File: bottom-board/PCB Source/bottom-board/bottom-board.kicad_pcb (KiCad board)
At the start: 4 copper layers, 193 x 93 mm, 307 parts, among them J1 AS0A823-H4SB-7H, P1 USB_B, P10 JACK_TRS_6PINS, P11 JACK_TRS_6PINS, P12 JACK_TRS_6PINS, P13 RJ45, P14 AudioJack3, P2 USB_A, P3 BARREL_JACK, P5 HMI_DATA, P6 AudioJack3, P7 AudioJack3, P8 SERIAL_DEBUG, P9 JACK_TRS_6PINS, Q1 2N7002, Q10 MMBFJ111, Q12 2N7002, Q13 2N7002, Q2 2N7002, Q3 MMBFJ111, Q4 MMBFJ111, Q5 MMBFJ111, Q6 MMBFJ111, Q7 2N7002, Q8 2N7002, Q9 MMBFJ111, U1 TS2596, U10 TPS2001DDBVR, U11 6N137S, U12 ISL83491, U13 AP2120N-3.3, U2 TL750M10CKVURG3, U3 CS4265, U4 AT24CS08-STUM, U5 LM4562, U6 OPA1678, U7 OPA1678, U8 LM4811, U9 LD1117S50TR_SOT223, X1 24.576MHz

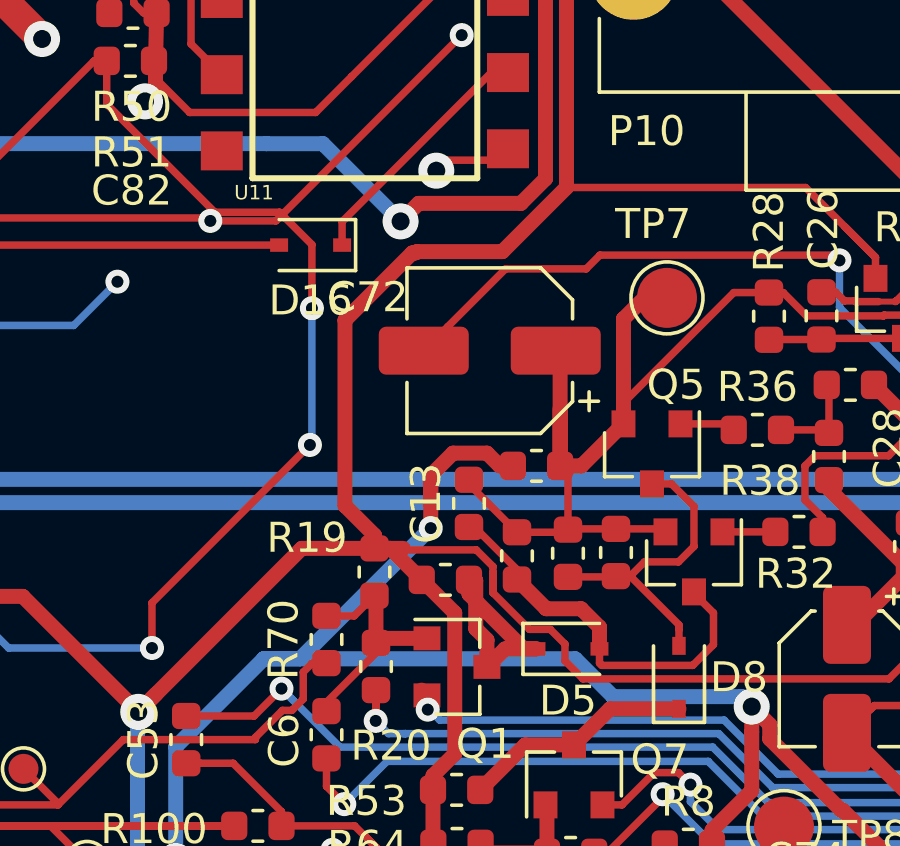
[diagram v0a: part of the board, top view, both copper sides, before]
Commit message: change input bias from 5 to 6 volts
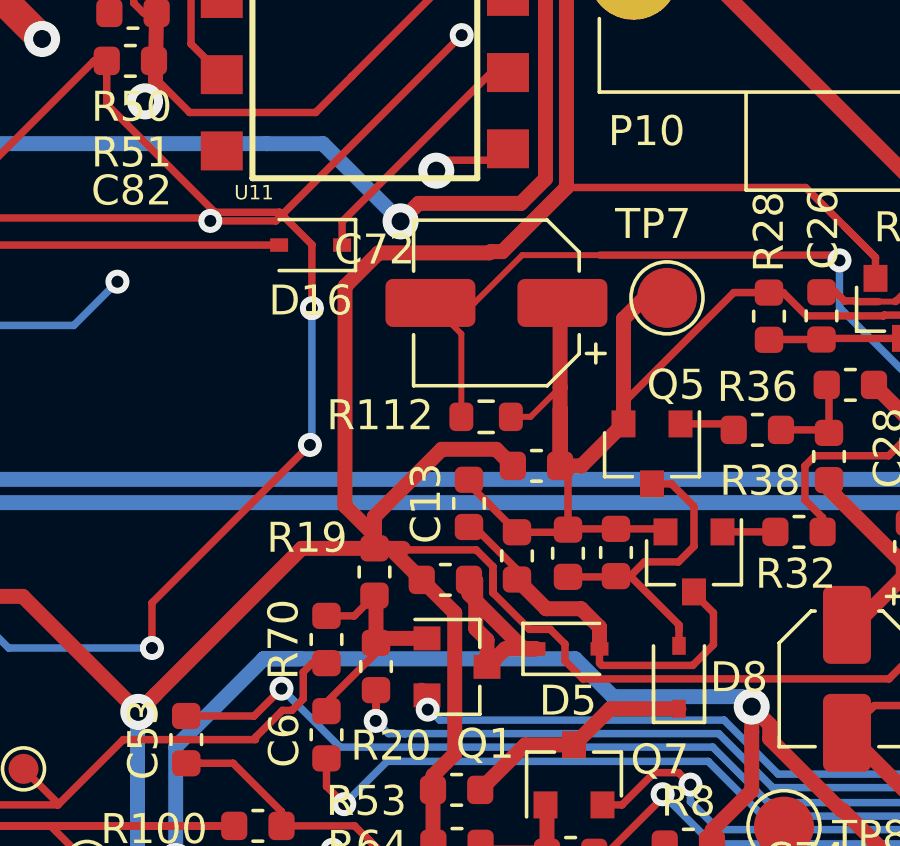
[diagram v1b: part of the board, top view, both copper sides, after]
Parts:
- added R112: 1K, Resistor_SMD:R_0603_1608Metric, F.Cu at (202.6, 75.9)
- C21, C23: value 100nF -> 100pF
- Q10, Q3, Q4, Q5, Q6, Q9: value MMBFJ111 -> MMBFJ110
- R101: value 100R -> 1K
- moved C72 1.61 mm to (202.9, 72.1)
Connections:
- R101 pad 2: +5VA -> +10V
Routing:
- net +5VA: track 290.0 -> 277.8 mm, vias 15 -> 14
- net +10V: track 311.8 -> 319.3 mm
- net INPUT_BIAS: track 88.5 -> 92.1 mm
- net GNDA: track 3561.3 -> 3564.7 mm

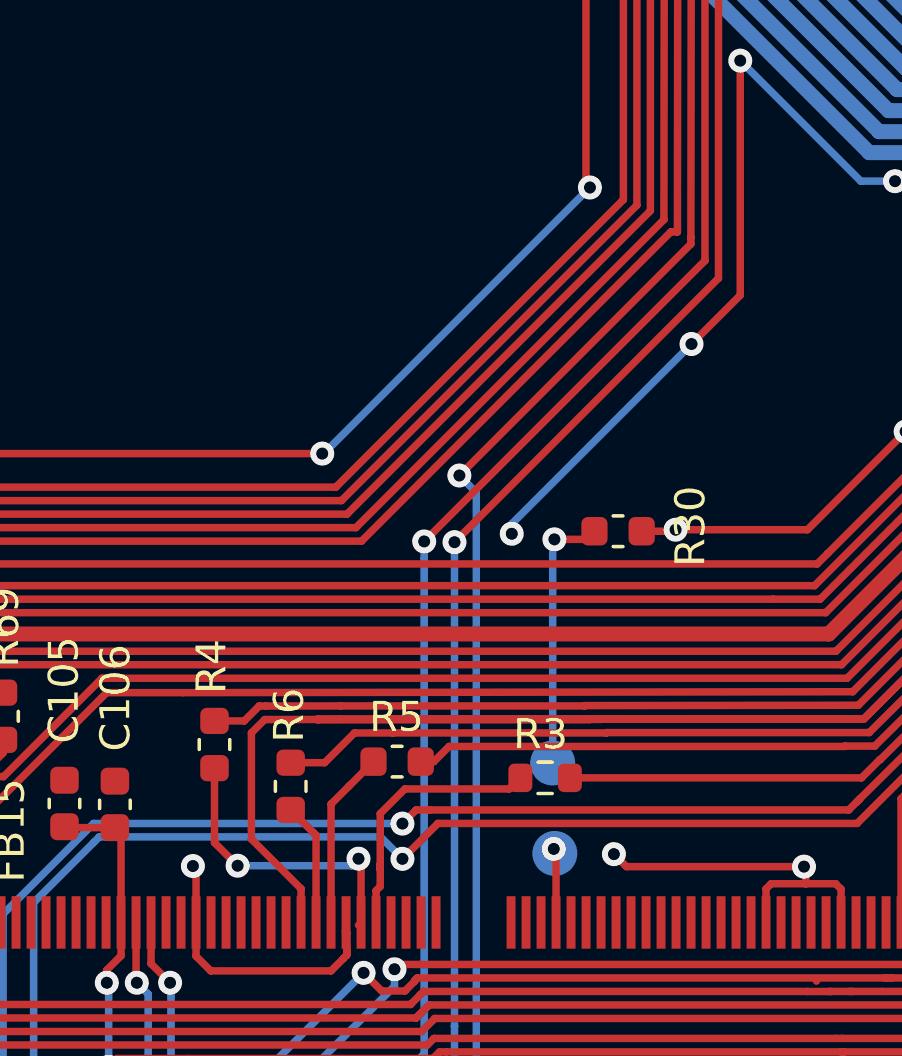
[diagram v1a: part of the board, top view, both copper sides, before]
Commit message: change recovery pads to holes, easier on production
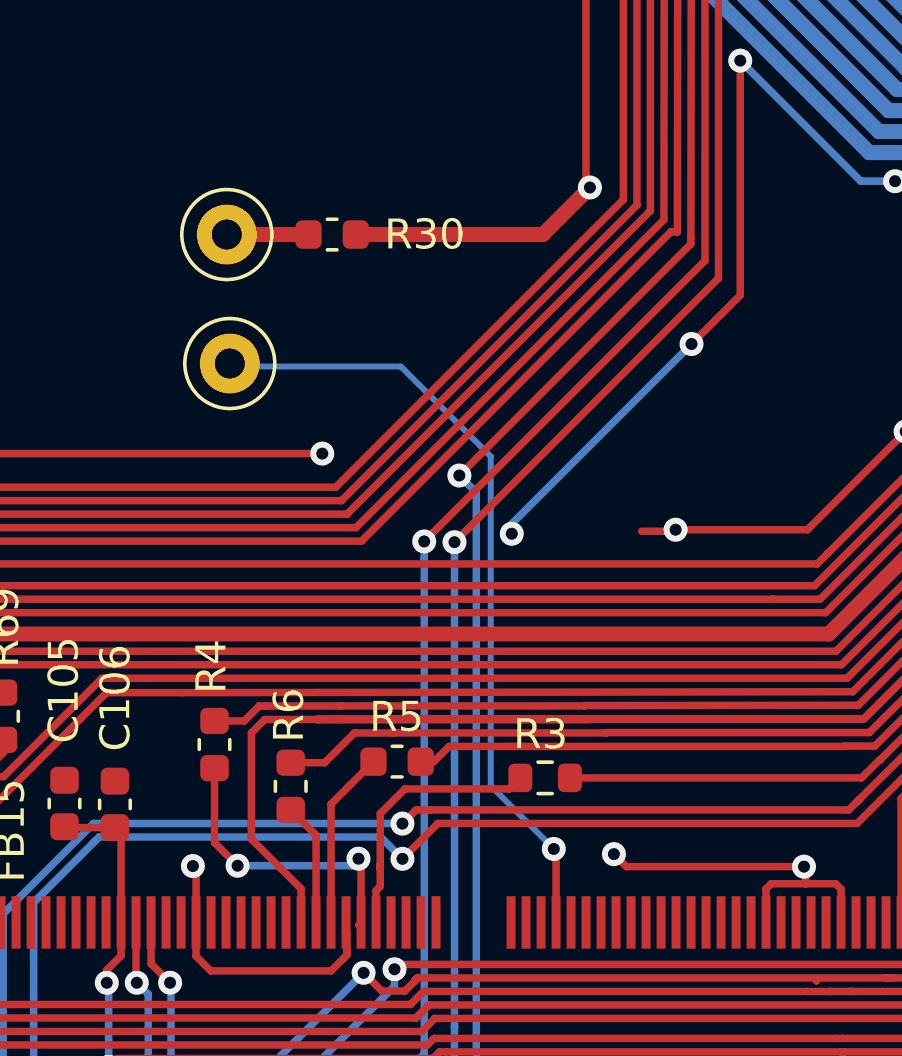
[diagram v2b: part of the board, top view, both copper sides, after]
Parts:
- removed Reset1: TestPoint, TestPoint:TestPoint_Pad_D1.5mm
- added Reset: TestPoint, TestPoint:TestPoint_Pad_D1.5mm, B.Cu at (120.3, 130.3)
- TP1, TP2: footprint TestPoint:TestPoint_Pad_D1.5mm -> TestPoint:TestPoint_Loop_D1.80mm_Drill1.0mm_Beaded; moved to F.Cu
- moved TP2 20.7 mm to (98.2, 101.2)
- moved TP1 19.6 mm to (98.3, 105.5)
- moved R30 13.7 mm to (101.7, 101.2)
- renumbered Power1 to Power
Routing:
- net UBOOT_BUTTON: track 2.50 -> 26.8 mm
- net Net-(R30-Pad2): track 8.93 -> 3.12 mm, vias 1 -> 0
- net GNDD: track 1451.8 -> 1447.7 mm

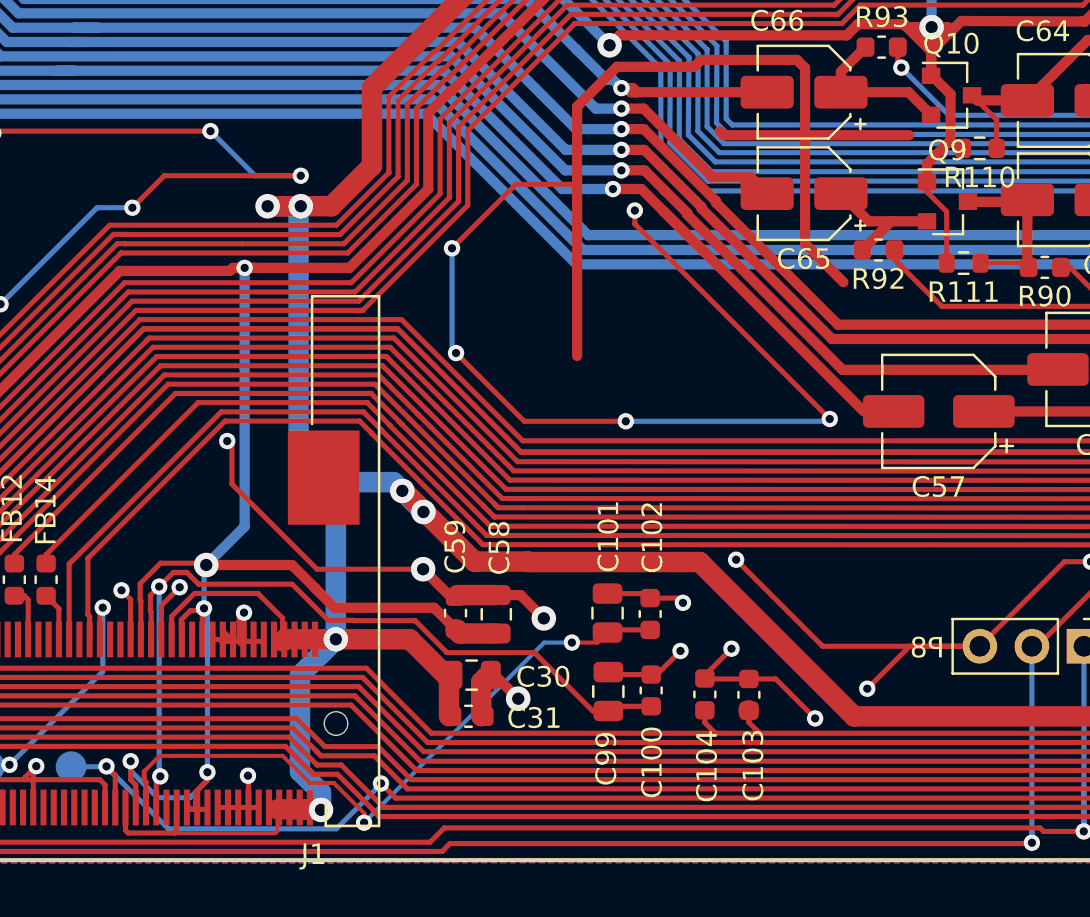
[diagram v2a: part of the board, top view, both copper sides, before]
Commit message: give analog bias to PX30 analog reference
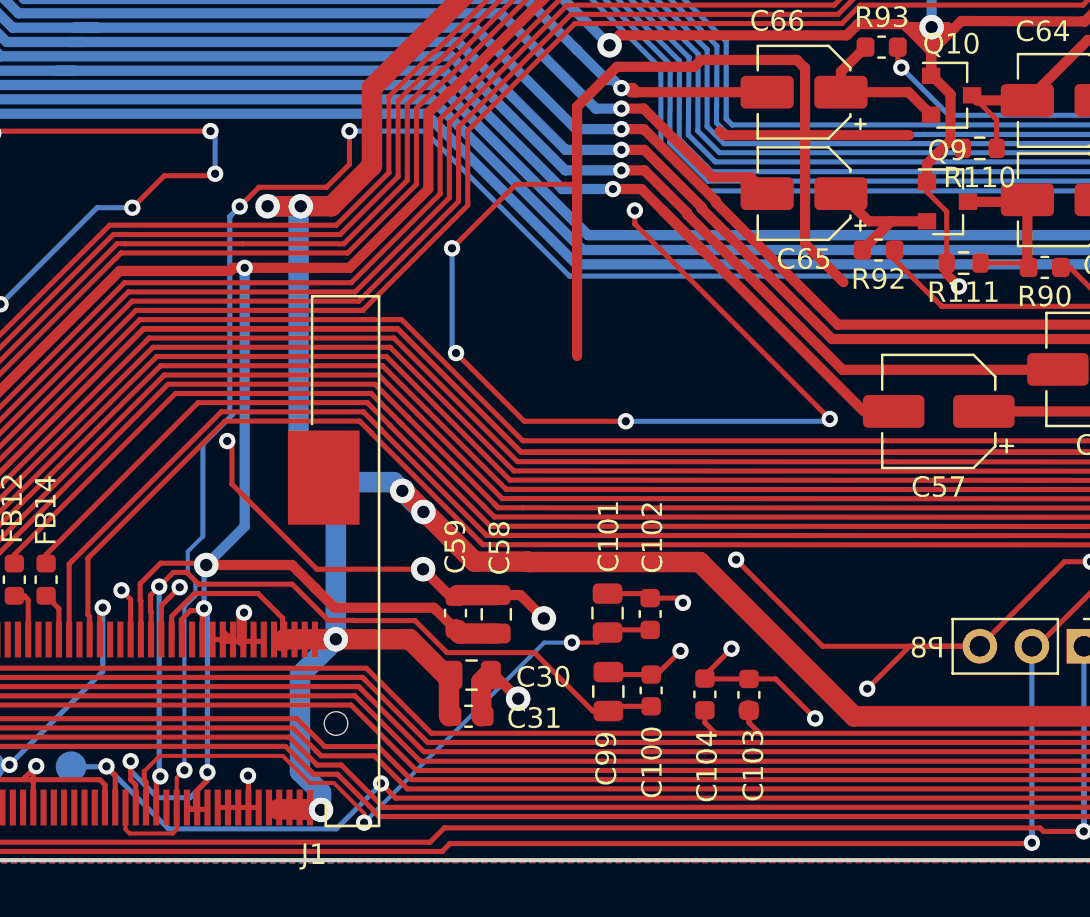
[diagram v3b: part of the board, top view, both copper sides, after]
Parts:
- renumbered Power to Power1, Reset to Reset1
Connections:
- J1 pad 223: +5V -> +5VA
- J1 pad 233: +5V -> +5VA
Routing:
- net +5VA: track 277.8 -> 356.4 mm, vias 14 -> 18
- net +5V: track 219.9 -> 209.2 mm
- net GNDD: track 1447.7 -> 1440.4 mm
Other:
- board text added: "MOD Devices GmbH http://moddevices.com [MDW-ELE-001] MOD Dwarf - Main Board Rev.: MDW-PX30-V1.05 Date: 2021.XXXX"
- board text removed: "MOD Devices GmbH http://moddevices.com [MDW-ELE-001] MOD Dwarf - Main Board Rev.: MDW-PX30-V1.00 Date: 2020.12.23"
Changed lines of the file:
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@@
     (thickness 1.6)
     (drawings 354)
-    (tracks 4338)
+    (tracks 4363)
     (zones 0)
     (modules 308)
@@
   )
   (setup
-    (last_trace_width 0.2)
+    (last_trace_width 0.25)
     (user_trace_width 0.2)
     (user_trace_width 0.45)
@@
     (tags "test point SMD pad")
     (attr virtual)
-    (fp_text reference Power (at 0.07 -2.13) (layer B.SilkS)
+    (fp_text reference Power1 (at 0.07 -2.13) (layer B.SilkS)
       (effects (font (size 1 1) (thickness 0.15)) (justify mirror))
     )
@@
     (tags "test point SMD pad")
     (attr virtual)
-    (fp_text reference Reset (at -0.06 2.38) (layer B.SilkS)
+    (fp_text reference Reset1 (at -0.06 2.38) (layer B.SilkS)
       (effects (font (size 1 1) (thickness 0.15)) (justify mirror))
     )
@@
     (pad 222 smd rect (at -20.375 4.1 180) (size 0.3 1.75) (layers F.Cu F.Paste F.Mask))
     (pad 223 smd rect (at -20.625 -4.1 180) (size 0.3 1.75) (layers F.Cu F.Paste F.Mask)
-      (net 3 +5V))
+      (net 4 +5VA))
     (pad 224 smd rect (at -20.875 4.1 180) (size 0.3 1.75) (layers F.Cu F.Paste F.Mask)
       (net 64 GNDD))
@@
       (net 3 +5V))
     (pad 233 smd rect (at -23.125 -4.1 180) (size 0.3 1.75) (layers F.Cu F.Paste F.Mask)
-      (net 3 +5V))
+      (net 4 +5VA))
     (pad 234 smd rect (at -23.375 4.1 180) (size 0.3 1.75) (layers F.Cu F.Paste F.Mask)
       (net 11 +3V3))
@@
   (gr_line (start 70.25768 124.05788) (end 70.10768 124.05788) (layer Dwgs.User) (width 0.2))
   (gr_line (start 135.65768 117.75788) (end 137.80768 117.75788) (layer Dwgs.User) (width 0.2))
-  (gr_text "MOD Devices GmbH\nhttp://moddevices.com\n\n[MDW-ELE-001]\nMOD Dwarf - Main Board \nRev.: MDW-PX30-V1.00\nDate: 2020.12.23" (at 244.76 117.31) (layer B.SilkS)
+  (gr_text "MOD Devices GmbH\nhttp://moddevices.com\n\n[MDW-ELE-001]\nMOD Dwarf - Main Board \nRev.: MDW-PX30-V1.05\nDate: 2021.XXXX" (at 244.76 117.31) (layer B.SilkS)
     (effects (font (size 1.5 1.5) (thickness 0.3)) (justify left mirror))
   )
@@
   (via (at 203.3 57.84) (size 1.2) (drill 0.6) (layers F.Cu B.Cu) (net 3))
   (segment (start 203.3 59.31) (end 203.3 57.84) (width 0.5) (layer F.Cu) (net 3))
-  (segment (start 134.35 132.44) (end 134.35 133.515) (width 0.2) (layer F.Cu) (net 3))
-  (segment (start 134.35 133.515) (end 134.249999 133.615001) (width 0.2) (layer F.Cu) (net 3))
-  (segment (start 134.249999 133.615001) (end 129.365001 133.615001) (width 0.2) (layer F.Cu) (net 3))
-  (segment (start 129.35 133.6) (end 129.365001 133.615001) (width 0.2) (layer F.Cu) (net 3))
   (segment (start 129.185 123.03) (end 130.305 121.91) (width 0.25) (layer F.Cu) (net 3))
   (segment (start 129.185 124.16) (end 129.185 123.03) (width 0.25) (layer F.Cu) (net 3))
-  (segment (start 129.346981 133.603019) (end 129.35 133.6) (width 0.25) (layer F.Cu) (net 3))
-  (segment (start 127.068017 133.603019) (end 129.346981 133.603019) (width 0.25) (layer F.Cu) (net 3))
-  (segment (start 126.935 133.470002) (end 127.068017 133.603019) (width 0.25) (layer F.Cu) (net 3))
-  (segment (start 126.935 132.36) (end 126.935 133.470002) (width 0.25) (layer F.Cu) (net 3))
-  (segment (start 129.346981 133.558021) (end 129.42198 133.483022) (width 0.25) (layer F.Cu) (net 3))
-  (segment (start 129.346981 133.603019) (end 129.346981 133.558021) (width 0.25) (layer F.Cu) (net 3))
-  (segment (start 129.42198 132.65839) (end 129.410001 132.646411) (width 0.25) (layer F.Cu) (net 3))
-  (segment (start 129.42198 133.483022) (end 129.42198 132.65839) (width 0.25) (layer F.Cu) (net 3))
+  (segment (start 129.42198 132.65839) (end 129.410001 132.646411) (width 0.25) (layer F.Cu) (net 4))
   (via (at 140.444516 116.905484) (size 1.2) (drill 0.6) (layers F.Cu B.Cu) (net 3))
   (segment (start 140.019032 116.48) (end 140.444516 116.905484) (width 1) (layer B.Cu) (net 3))
@@
   (segment (start 167.59124 100.19124) (end 167.2 99.8) (width 0.25) (layer F.Cu) (net 4))
   (segment (start 167.79884 100.19124) (end 167.59124 100.19124) (width 0.25) (layer F.Cu) (net 4))
+  (segment (start 127.138017 133.628019) (end 126.935 133.425002) (width 0.2) (layer F.Cu) (net 4))
+  (segment (start 129.241981 133.628019) (end 127.138017 133.628019) (width 0.2) (layer F.Cu) (net 4))
+  (segment (start 129.435 133.435) (end 129.241981 133.628019) (width 0.2) (layer F.Cu) (net 4))
+  (segment (start 126.935 133.425002) (end 126.935 132.36) (width 0.2) (layer F.Cu) (net 4))
+  (segment (start 129.435 132.36) (end 129.435 133.435) (width 0.2) (layer F.Cu) (net 4))
+  (via (at 129.81 130.539989) (size 0.8) (drill 0.4) (layers F.Cu B.Cu) (net 4))
+  (segment (start 129.435 130.914989) (end 129.81 130.539989) (width 0.2) (layer F.Cu) (net 4))
+  (segment (start 129.435 132.36) (end 129.435 130.914989) (width 0.2) (layer F.Cu) (net 4))
+  (segment (start 129.974999 119.865001) (end 130.71 119.13) (width 0.2) (layer B.Cu) (net 4))
+  (segment (start 129.974999 120.957001) (end 129.974999 119.865001) (width 0.2) (layer B.Cu) (net 4))
+  (segment (start 130.34499 121.326992) (end 129.974999 120.957001) (width 0.2) (layer B.Cu) (net 4))
+  (segment (start 130.34499 122.024408) (end 130.34499 121.326992) (width 0.2) (layer B.Cu) (net 4))
+  (segment (start 129.81 122.559398) (end 130.34499 122.024408) (width 0.2) (layer B.Cu) (net 4))
+  (segment (start 129.81 130.539989) (end 129.81 122.559398) (width 0.2) (layer B.Cu) (net 4))
+  (via (at 167.61 106.93) (size 0.8) (drill 0.4) (layers F.Cu B.Cu) (net 4))
+  (segment (start 167.01144 106.33144) (end 167.61 106.93) (width 0.45) (layer F.Cu) (net 4))
+  (segment (start 167.01144 105.7894) (end 167.01144 106.33144) (width 0.45) (layer F.Cu) (net 4))
+  (segment (start 167.61 106.93) (end 167.20501 106.52501) (width 0.45) (layer B.Cu) (net 4))
+  (segment (start 130.71 114.63) (end 132.17499 113.16501) (width 0.25) (layer B.Cu) (net 4))
+  (segment (start 130.71 119.13) (end 130.71 114.63) (width 0.25) (layer B.Cu) (net 4))
+  (segment (start 132.17499 113.16501) (end 132.024999 113.015019) (width 0.25) (layer B.Cu) (net 4))
+  (segment (start 167.10501 106.42501) (end 167.61 106.93) (width 0.25) (layer B.Cu) (net 4))
+  (segment (start 148.60501 106.42501) (end 167.10501 106.42501) (width 0.25) (layer B.Cu) (net 4))
+  (via (at 132.51 103.03) (size 0.8) (drill 0.4) (layers F.Cu B.Cu) (net 4))
+  (segment (start 132.024999 103.515001) (end 132.51 103.03) (width 0.25) (layer B.Cu) (net 4))
+  (segment (start 132.024999 103.544999) (end 132.024999 103.515001) (width 0.25) (layer B.Cu) (net 4))
+  (segment (start 132.024999 113.015019) (end 132.024999 103.544999) (width 0.25) (layer B.Cu) (net 4))
+  (segment (start 133.45003 102.08997) (end 136.74373 102.08997) (width 0.25) (layer F.Cu) (net 4))
+  (segment (start 132.51 103.03) (end 133.45003 102.08997) (width 0.25) (layer F.Cu) (net 4))
+  (via (at 137.863657 99.35) (size 0.8) (drill 0.4) (layers F.Cu B.Cu) (net 4))
+  (segment (start 137.863657 100.970043) (end 137.863657 99.35) (width 0.25) (layer F.Cu) (net 4))
+  (segment (start 136.74373 102.08997) (end 137.863657 100.970043) (width 0.25) (layer F.Cu) (net 4))
+  (segment (start 141.53 99.35) (end 141.56 99.38) (width 0.25) (layer B.Cu) (net 4))
+  (segment (start 137.863657 99.35) (end 141.53 99.35) (width 0.25) (layer B.Cu) (net 4))
+  (segment (start 141.56 99.38) (end 148.60501 106.42501) (width 0.25) (layer B.Cu) (net 4))
   (segment (start 221.65 98.55) (end 222.5625 98.55) (width 0.25) (layer F.Cu) (net 5))
   (segment (start 227.875 98.55) (end 227.4375 98.55) (width 0.25) (layer F.Cu) (net 5))
@@
   (segment (start 125.54712 103.08844) (end 127.26924 103.08844) (width 0.25) (layer B.Cu) (net 64))
   (segment (start 120.83796 107.7976) (end 125.54712 103.08844) (width 0.25) (layer B.Cu) (net 64))
-  (via (at 135.48868 101.52634) (size 0.8) (drill 0.4) (layers F.Cu B.Cu) (net 64))
-  (segment (start 128.83134 101.52634) (end 135.48868 101.52634) (width 0.25) (layer F.Cu) (net 64))
   (segment (start 127.26924 103.08844) (end 128.83134 101.52634) (width 0.25) (layer F.Cu) (net 64))
   (via (at 131.08432 99.35) (size 0.8) (drill 0.4) (layers F.Cu B.Cu) (net 64))
-  (segment (start 133.26066 101.52634) (end 131.08432 99.35) (width 0.25) (layer B.Cu) (net 64))
-  (segment (start 135.48868 101.52634) (end 133.26066 101.52634) (width 0.25) (layer B.Cu) (net 64))
   (via (at 120.4849 99.45116) (size 0.8) (drill 0.4) (layers F.Cu B.Cu) (net 64))
   (segment (start 120.58606 99.35) (end 120.4849 99.45116) (width 0.25) (layer F.Cu) (net 64))
@@
   (segment (start 108.74672 101.23) (end 110.31474 99.66198) (width 0.5) (layer F.Cu) (net 64))
   (segment (start 102.51 101.23) (end 108.74672 101.23) (width 0.5) (layer F.Cu) (net 64))
+  (via (at 131.31 101.43) (size 0.8) (drill 0.4) (layers F.Cu B.Cu) (net 64))
+  (segment (start 131.21366 101.52634) (end 131.31 101.43) (width 0.25) (layer F.Cu) (net 64))
+  (segment (start 128.83134 101.52634) (end 131.21366 101.52634) (width 0.25) (layer F.Cu) (net 64))
+  (segment (start 131.31 99.57568) (end 131.08432 99.35) (width 0.25) (layer B.Cu) (net 64))
+  (segment (start 131.31 101.43) (end 131.31 99.57568) (width 0.25) (layer B.Cu) (net 64))
   (segment (start 225.75 94.740568) (end 227.090568 93.4) (width 0.25) (layer F.Cu) (net 65))
   (segment (start 227.090568 93.4) (end 227.4 93.4) (width 0.25) (layer F.Cu) (net 65))
